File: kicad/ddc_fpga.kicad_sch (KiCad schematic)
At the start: 10 parts, among them U13 ICE40UP5K-SG48ITR

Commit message: updates
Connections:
- net CLK_DDC: now reaches U13.35 (IOT_46b_G0)
- net TOS_MARK_DDC: now reaches U13.37 (IOT_45a_G1)
- net DDC_I2S_WS: now reaches U13.10 (IOB_18a)
- net DDC_I2S_SD: now reaches U13.11 (IOB_20a)
- net DDC_RESET_L: now reaches U13.20 (IOB_25b_G3)
- net DDC_I2S_SCK: now reaches U13.9 (IOB_16a)
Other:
- moved on the sheet: C31, U13A
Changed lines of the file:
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@@
   (junction (at 147.32 147.32) (diameter 0) (color 0 0 0 0)
   )
-  (junction (at 44.45 115.57) (diameter 0) (color 0 0 0 0)
+  (junction (at 62.23 115.57) (diameter 0) (color 0 0 0 0)
   )
   (junction (at 101.6 151.13) (diameter 0) (color 0 0 0 0)
@@
   (junction (at 87.63 50.8) (diameter 0) (color 0 0 0 0)
   )
+  (wire (pts (xy 179.07 77.47) (xy 204.47 77.47))
+    (stroke (width 0) (type default))
+  )
   (wire (pts (xy 54.61 81.28) (xy 77.47 81.28))
     (stroke (width 0) (type default))
   )
+  (wire (pts (xy 179.07 80.01) (xy 204.47 80.01))
+    (stroke (width 0) (type default))
+  )
   (wire (pts (xy 118.11 132.08) (xy 118.11 153.67))
     (stroke (width 0) (type default))
@@
     (stroke (width 0) (type default))
   )
-  (wire (pts (xy 44.45 115.57) (xy 44.45 128.27))
+  (wire (pts (xy 62.23 115.57) (xy 62.23 128.27))
     (stroke (width 0) (type default))
   )
@@
     (stroke (width 0) (type default))
   )
-  (wire (pts (xy 50.8 115.57) (xy 44.45 115.57))
+  (wire (pts (xy 68.58 115.57) (xy 62.23 115.57))
     (stroke (width 0) (type default))
   )
@@
     (stroke (width 0) (type default))
   )
-  (wire (pts (xy 50.8 116.84) (xy 50.8 115.57))
+  (wire (pts (xy 68.58 116.84) (xy 68.58 115.57))
     (stroke (width 0) (type default))
   )
@@
     (stroke (width 0) (type default))
   )
+  (wire (pts (xy 36.83 161.29) (xy 52.07 161.29))
+    (stroke (width 0) (type default))
+  )
   (wire (pts (xy 123.19 132.08) (xy 118.11 132.08))
     (stroke (width 0) (type default))
@@
     (stroke (width 0) (type default))
   )
-  (wire (pts (xy 44.45 114.3) (xy 44.45 115.57))
+  (wire (pts (xy 179.07 90.17) (xy 204.47 90.17))
+    (stroke (width 0) (type default))
+  )
+  (wire (pts (xy 62.23 114.3) (xy 62.23 115.57))
     (stroke (width 0) (type default))
   )
@@
   )
   (wire (pts (xy 172.72 43.18) (xy 172.72 41.91))
+    (stroke (width 0) (type default))
+  )
+  (wire (pts (xy 36.83 163.83) (xy 52.07 163.83))
+    (stroke (width 0) (type default))
+  )
+  (wire (pts (xy 179.07 74.93) (xy 204.47 74.93))
     (stroke (width 0) (type default))
   )
@@
   (label "DDC_MISO_OUT" (at 181.61 97.79 0) (fields_autoplaced)
     (effects (font (size 1.27 1.27)) (justify left bottom))
+  )
+  (global_label "DDC_RESET_L" (shape input) (at 204.47 90.17 0) (fields_autoplaced)
+    (effects (font (size 1.27 1.27)) (justify left))
+    (property "Intersheetrefs" "${INTERSHEET_REFS}" (at 219.9736 90.17 0)
+      (effects (font (size 1.27 1.27)) (justify left) hide)
+    )
   )
   (global_label "DDC_SCK" (shape input) (at 208.28 102.87 0) (fields_autoplaced)
@@
     )
   )
+  (global_label "CLK_DDC" (shape input) (at 36.83 163.83 180) (fields_autoplaced)
+    (effects (font (size 1.27 1.27)) (justify right))
+    (property "Intersheetrefs" "${INTERSHEET_REFS}" (at 25.4991 163.83 0)
+      (effects (font (size 1.27 1.27)) (justify right) hide)
+    )
+  )
+  (global_label "DDC_I2S_WS" (shape output) (at 204.47 77.47 0) (fields_autoplaced)
+    (effects (font (size 1.27 1.27)) (justify left))
+    (property "Intersheetrefs" "${INTERSHEET_REFS}" (at 218.8851 77.47 0)
+      (effects (font (size 1.27 1.27)) (justify left) hide)
+    )
+  )
   (global_label "DDC_CRST" (shape input) (at 204.47 64.77 0) (fields_autoplaced)
     (effects (font (size 1.27 1.27)) (justify left))
@@
     )
   )
+  (global_label "DDC_I2S_SCK" (shape output) (at 204.47 74.93 0) (fields_autoplaced)
+    (effects (font (size 1.27 1.27)) (justify left))
+    (property "Intersheetrefs" "${INTERSHEET_REFS}" (at 219.9737 74.93 0)
+      (effects (font (size 1.27 1.27)) (justify left) hide)
+    )
+  )
   (global_label "ADC_SCK_P" (shape input) (at 54.61 78.74 180) (fields_autoplaced)
     (effects (font (size 1.27 1.27)) (justify right))
@@
     )
   )
+  (global_label "DDC_I2S_SD" (shape output) (at 204.47 80.01 0) (fields_autoplaced)
+    (effects (font (size 1.27 1.27)) (justify left))
+    (property "Intersheetrefs" "${INTERSHEET_REFS}" (at 218.7037 80.01 0)
+      (effects (font (size 1.27 1.27)) (justify left) hide)
+    )
+  )
   (global_label "ADC_SCK_N" (shape input) (at 54.61 81.28 180) (fields_autoplaced)
     (effects (font (size 1.27 1.27)) (justify right))
     (property "Intersheetrefs" "${INTERSHEET_REFS}" (at 40.981 81.28 0)
+      (effects (font (size 1.27 1.27)) (justify right) hide)
+    )
+  )
+  (global_label "TOS_MARK_DDC" (shape input) (at 36.83 161.29 180) (fields_autoplaced)
+    (effects (font (size 1.27 1.27)) (justify right))
+    (property "Intersheetrefs" "${INTERSHEET_REFS}" (at 19.512 161.29 0)
       (effects (font (size 1.27 1.27)) (justify right) hide)
     )
@@
   )
   (symbol (lib_id "Device:R_US") (at 199.39 97.79 90) (unit 1)
-    (in_bom yes) (on_board yes) (dnp no) (fields_autoplaced)
-    (property "Reference" "R23" (at 199.39 91.44 90)
-      (effects (font (size 1.27 1.27)))
-    )
-    (property "Value" "22" (at 199.39 93.98 90)
+    (in_bom yes) (on_board yes) (dnp no)
+    (property "Reference" "R23" (at 199.39 92.71 90)
+      (effects (font (size 1.27 1.27)))
+    )
+    (property "Value" "22" (at 199.39 95.25 90)
       (effects (font (size 1.27 1.27)))
     )
@@
     )
   )
-  (symbol (lib_id "power:+3.3V") (at 44.45 114.3 0) (unit 1)
-    (in_bom yes) (on_board yes) (dnp no) (fields_autoplaced)
-    (property "Reference" "#PWR068" (at 44.45 118.11 0)
-      (effects (font (size 1.27 1.27)) hide)
-    )
-    (property "Value" "+3.3V" (at 44.45 109.22 0)
-      (effects (font (size 1.27 1.27)))
-    )
-    (property "Footprint" "" (at 44.45 114.3 0)
-      (effects (font (size 1.27 1.27)) hide)
-    )
-    (property "Datasheet" "" (at 44.45 114.3 0)
+  (symbol (lib_id "power:+3.3V") (at 62.23 114.3 0) (unit 1)
+    (in_bom yes) (on_board yes) (dnp no) (fields_autoplaced)
+    (property "Reference" "#PWR068" (at 62.23 118.11 0)
+      (effects (font (size 1.27 1.27)) hide)
+    )
+    (property "Value" "+3.3V" (at 62.23 109.22 0)
+      (effects (font (size 1.27 1.27)))
+    )
+    (property "Footprint" "" (at 62.23 114.3 0)
+      (effects (font (size 1.27 1.27)) hide)
+    )
+    (property "Datasheet" "" (at 62.23 114.3 0)
       (effects (font (size 1.27 1.27)) hide)
     )
@@
     )
   )
-  (symbol (lib_id "FPGA_Lattice:ICE40UP5K-SG48ITR") (at 44.45 156.21 0) (unit 1)
-    (in_bom yes) (on_board yes) (dnp no) (fields_autoplaced)
-    (property "Reference" "U13" (at 53.34 156.21 0)
-      (effects (font (size 1.27 1.27)) (justify left))
-    )
-    (property "Value" "ICE40UP5K-SG48ITR" (at 53.34 158.75 0)
-      (effects (font (size 1.27 1.27)) (justify left))
-    )
-    (property "Footprint" "Package_DFN_QFN:QFN-48-1EP_7x7mm_P0.5mm_EP5.1x5.1mm" (at 44.45 190.5 0)
-      (effects (font (size 1.27 1.27)) hide)
-    )
-    (property "Datasheet" "http://www.latticesemi.com/Products/FPGAandCPLD/iCE40Ultra" (at 34.29 130.81 0)
+  (symbol (lib_id "FPGA_Lattice:ICE40UP5K-SG48ITR") (at 62.23 156.21 0) (unit 1)
+    (in_bom yes) (on_board yes) (dnp no) (fields_autoplaced)
+    (property "Reference" "U13" (at 71.12 156.21 0)
+      (effects (font (size 1.27 1.27)) (justify left))
+    )
+    (property "Value" "ICE40UP5K-SG48ITR" (at 71.12 158.75 0)
+      (effects (font (size 1.27 1.27)) (justify left))
+    )
+    (property "Footprint" "Package_DFN_QFN:QFN-48-1EP_7x7mm_P0.5mm_EP5.1x5.1mm" (at 62.23 190.5 0)
+      (effects (font (size 1.27 1.27)) hide)
+    )
+    (property "Datasheet" "http://www.latticesemi.com/Products/FPGAandCPLD/iCE40Ultra" (at 52.07 130.81 0)
       (effects (font (size 1.27 1.27)) hide)
     )
@@
     )
   )
-  (symbol (lib_id "power:GND") (at 50.8 124.46 0) (unit 1)
-    (in_bom yes) (on_board yes) (dnp no) (fields_autoplaced)
-    (property "Reference" "#PWR069" (at 50.8 130.81 0)
-      (effects (font (size 1.27 1.27)) hide)
-    )
-    (property "Value" "GND" (at 50.8 129.54 0)
-      (effects (font (size 1.27 1.27)) hide)
-    )
-    (property "Footprint" "" (at 50.8 124.46 0)
-      (effects (font (size 1.27 1.27)) hide)
-    )
-    (property "Datasheet" "" (at 50.8 124.46 0)
+  (symbol (lib_id "power:GND") (at 68.58 124.46 0) (unit 1)
+    (in_bom yes) (on_board yes) (dnp no) (fields_autoplaced)
+    (property "Reference" "#PWR069" (at 68.58 130.81 0)
+      (effects (font (size 1.27 1.27)) hide)
+    )
+    (property "Value" "GND" (at 68.58 129.54 0)
+      (effects (font (size 1.27 1.27)) hide)
+    )
+    (property "Footprint" "" (at 68.58 124.46 0)
+      (effects (font (size 1.27 1.27)) hide)
+    )
+    (property "Datasheet" "" (at 68.58 124.46 0)
       (effects (font (size 1.27 1.27)) hide)
     )
@@
     )
   )
-  (symbol (lib_id "Device:C") (at 50.8 120.65 0) (unit 1)
-    (in_bom yes) (on_board yes) (dnp no) (fields_autoplaced)
-    (property "Reference" "C31" (at 54.61 119.38 0)
-      (effects (font (size 1.27 1.27)) (justify left))
-    )
-    (property "Value" "4.7u" (at 54.61 121.92 0)
-      (effects (font (size 1.27 1.27)) (justify left))
-    )
-    (property "Footprint" "" (at 51.7652 124.46 0)
-      (effects (font (size 1.27 1.27)) hide)
-    )
-    (property "Datasheet" "~" (at 50.8 120.65 0)
-      (effects (font (size 1.27 1.27)) hide)
-    )
+  (symbol (lib_id "Device:C") (at 68.58 120.65 0) (unit 1)
+    (in_bom yes) (on_board yes) (dnp no) (fields_autoplaced)
+    (property "Reference" "C31" (at 72.39 119.38 0)
+      (effects (font (size 1.27 1.27)) (justify left))
+    )
+    (property "Value" "4.7u" (at 72.39 121.92 0)
+      (effects (font (size 1.27 1.27)) (justify left))
+    )
+    (property "Footprint" "" (at 69.5452 124.46 0)
+      (effects (font (size 1.27 1.27)) hide)
+    )
+    (property "Datasheet" "~" (at 68.58 120.65 0)
+      (effects (font (size 1.27 1.27)) hide)
+    )

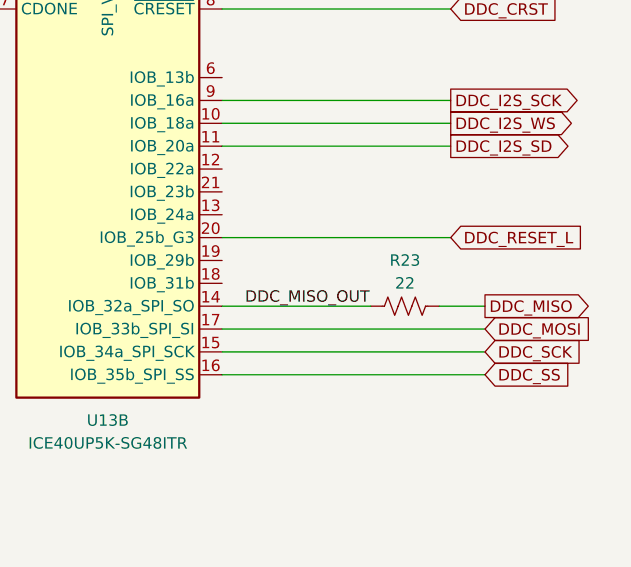
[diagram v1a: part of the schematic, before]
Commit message: wire up mcu
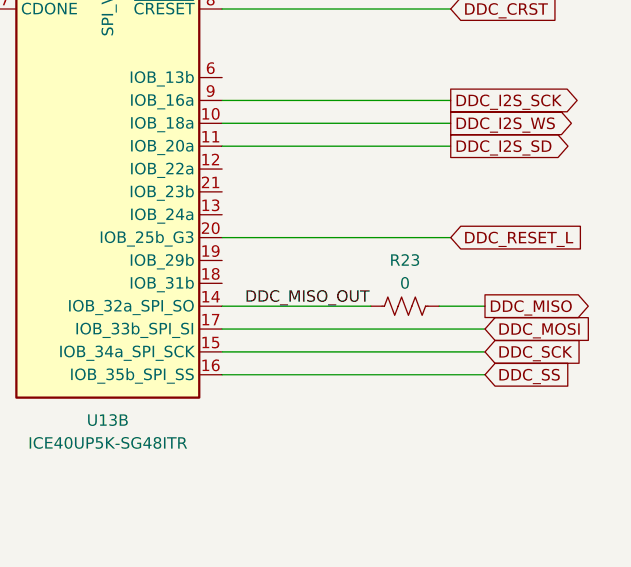
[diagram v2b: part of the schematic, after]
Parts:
- R23: value 22 -> 0
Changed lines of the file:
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@@
       (effects (font (size 1.27 1.27)))
     )
-    (property "Value" "22" (at 199.39 95.25 90)
+    (property "Value" "0" (at 199.39 95.25 90)
       (effects (font (size 1.27 1.27)))
     )

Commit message: fix ercs
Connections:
- net DDC_CRST renamed DDC_CRST_L
- no-connect marks 0 -> 24
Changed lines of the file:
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@@
   (junction (at 87.63 50.8) (diameter 0) (color 0 0 0 0)
   )
+  (no_connect (at 52.07 171.45))
+  (no_connect (at 52.07 148.59))
+  (no_connect (at 52.07 173.99))
+  (no_connect (at 52.07 156.21))
+  (no_connect (at 52.07 166.37))
+  (no_connect (at 77.47 91.44))
+  (no_connect (at 52.07 143.51))
+  (no_connect (at 77.47 93.98))
+  (no_connect (at 179.07 72.39))
+  (no_connect (at 52.07 140.97))
+  (no_connect (at 179.07 82.55))
+  (no_connect (at 179.07 87.63))
+  (no_connect (at 52.07 146.05))
+  (no_connect (at 179.07 85.09))
+  (no_connect (at 179.07 92.71))
+  (no_connect (at 52.07 158.75))
+  (no_connect (at 52.07 176.53))
+  (no_connect (at 52.07 181.61))
+  (no_connect (at 52.07 168.91))
+  (no_connect (at 52.07 153.67))
+  (no_connect (at 179.07 95.25))
+  (no_connect (at 52.07 179.07))
+  (no_connect (at 52.07 151.13))
+  (no_connect (at 77.47 88.9))
   (wire (pts (xy 179.07 77.47) (xy 204.47 77.47))
     (stroke (width 0) (type default))
@@
     )
   )
-  (global_label "DDC_CRST" (shape input) (at 204.47 64.77 0) (fields_autoplaced)
+  (global_label "DDC_CRST_L" (shape input) (at 204.47 64.77 0) (fields_autoplaced)
     (effects (font (size 1.27 1.27)) (justify left))
-    (property "Intersheetrefs" "${INTERSHEET_REFS}" (at 216.9499 64.77 0)
+    (property "Intersheetrefs" "${INTERSHEET_REFS}" (at 218.9456 64.77 0)
       (effects (font (size 1.27 1.27)) (justify left) hide)
     )

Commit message: power and frontend updates
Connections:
- net +3.3V renamed +3.3VP
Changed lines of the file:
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@@
     )
   )
-  (symbol (lib_id "power:+3.3V") (at 166.37 40.64 0) (unit 1)
+  (symbol (lib_id "power:+3.3VP") (at 62.23 114.3 0) (unit 1)
     (in_bom yes) (on_board yes) (dnp no) (fields_autoplaced)
-    (property "Reference" "#PWR066" (at 166.37 44.45 0)
+    (property "Reference" "#PWR068" (at 66.04 115.57 0)
       (effects (font (size 1.27 1.27)) hide)
     )
-    (property "Value" "+3.3V" (at 166.37 35.56 0)
+    (property "Value" "+3.3VP" (at 62.23 109.22 0)
+      (effects (font (size 1.27 1.27)))
+    )
+    (property "Footprint" "" (at 62.23 114.3 0)
+      (effects (font (size 1.27 1.27)) hide)
+    )
+    (property "Datasheet" "" (at 62.23 114.3 0)
+      (effects (font (size 1.27 1.27)) hide)
+    )
+    (pin "1")
+    (instances
+      (project "gpsrx"
+        (path "/c3c549bc-9d82-4b6a-bdb9-a3870905229d/c7ab4c42-2f90-4fd3-a6d5-50b84165476b"
+          (reference "#PWR068") (unit 1)
+        )
+      )
+    )
+  )
+  (symbol (lib_id "power:+3.3VP") (at 166.37 40.64 0) (unit 1)
+    (in_bom yes) (on_board yes) (dnp no) (fields_autoplaced)
+    (property "Reference" "#PWR066" (at 170.18 41.91 0)
+      (effects (font (size 1.27 1.27)) hide)
+    )
+    (property "Value" "+3.3VP" (at 166.37 35.56 0)
       (effects (font (size 1.27 1.27)))
     )
@@
         )
       )
-    )
-  )
-  (symbol (lib_id "power:+3.3V") (at 62.23 114.3 0) (unit 1)
-    (in_bom yes) (on_board yes) (dnp no) (fields_autoplaced)
-    (property "Reference" "#PWR068" (at 62.23 118.11 0)
-      (effects (font (size 1.27 1.27)) hide)
-    )
-    (property "Value" "+3.3V" (at 62.23 109.22 0)
-      (effects (font (size 1.27 1.27)))
-    )
-    (property "Footprint" "" (at 62.23 114.3 0)
-      (effects (font (size 1.27 1.27)) hide)
-    )
-    (property "Datasheet" "" (at 62.23 114.3 0)
-      (effects (font (size 1.27 1.27)) hide)
-    )
-    (pin "1")
-    (instances
-      (project "gpsrx"
-        (path "/c3c549bc-9d82-4b6a-bdb9-a3870905229d/c7ab4c42-2f90-4fd3-a6d5-50b84165476b"
-          (reference "#PWR068") (unit 1)
-        )
-      )

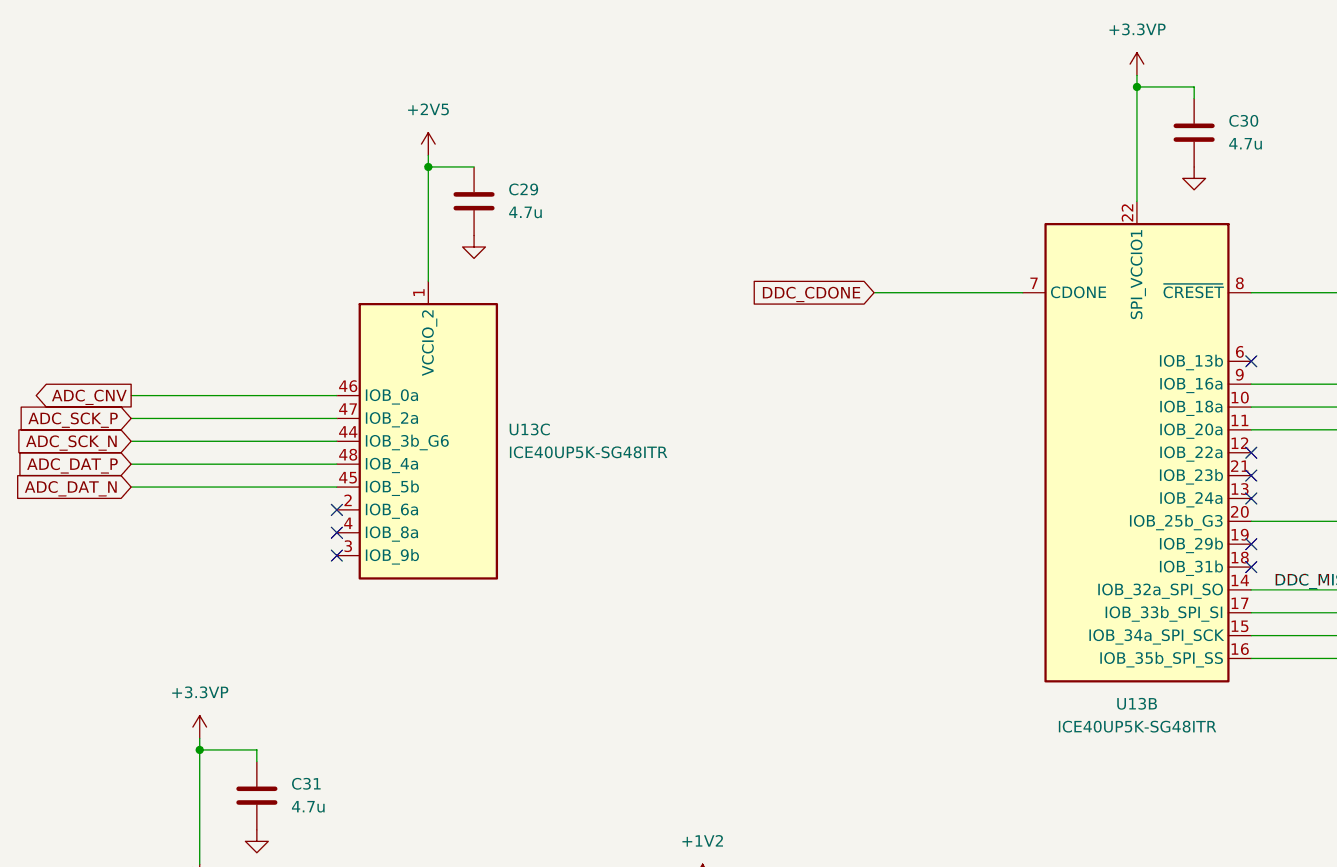
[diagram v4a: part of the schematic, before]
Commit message: swap ice40 for max v, add 1.2v switcher
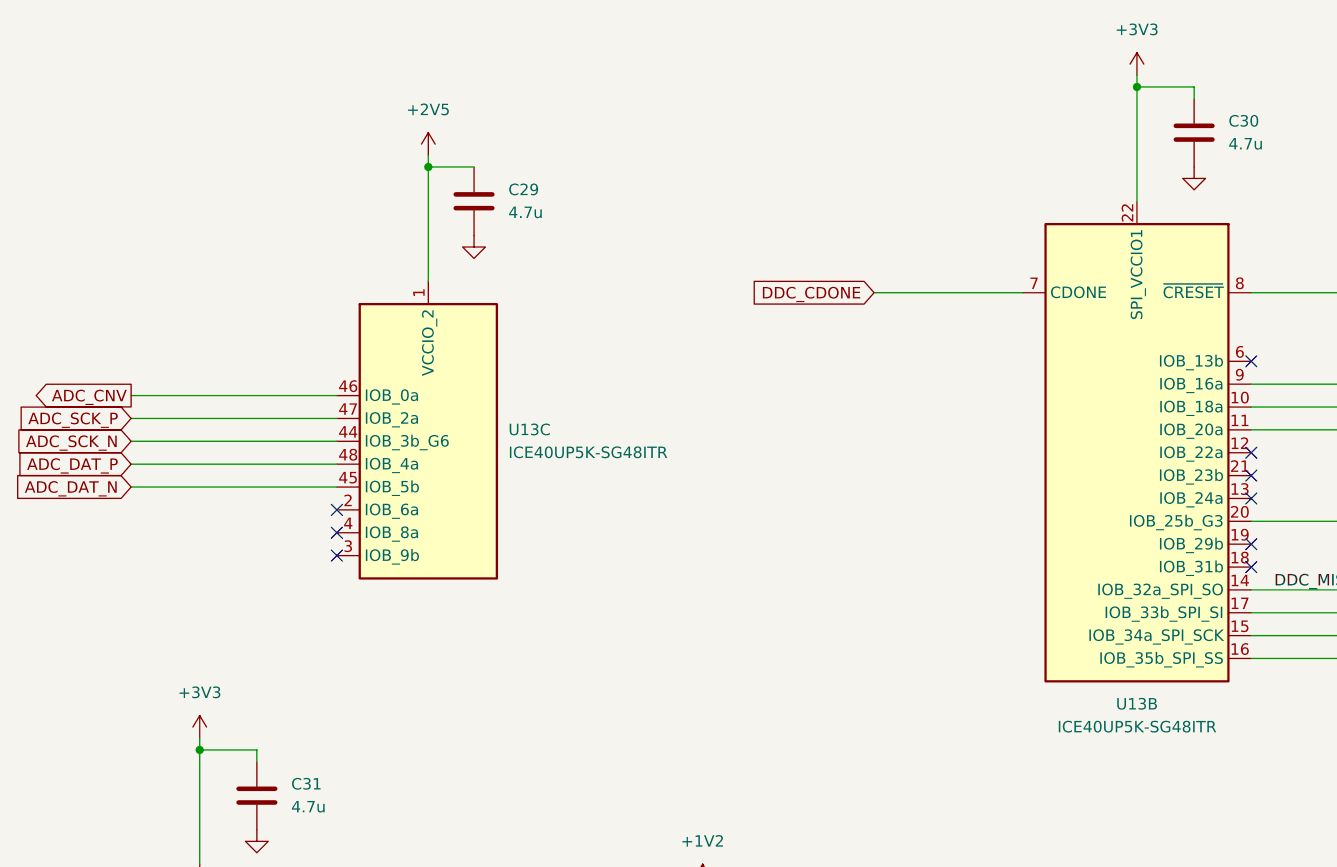
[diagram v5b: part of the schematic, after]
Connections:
- net +3.3VP renamed +3V3
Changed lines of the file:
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@@
     )
   )
-  (symbol (lib_id "power:+3.3VP") (at 62.23 114.3 0) (unit 1)
-    (in_bom yes) (on_board yes) (dnp no) (fields_autoplaced)
-    (property "Reference" "#PWR068" (at 66.04 115.57 0)
-      (effects (font (size 1.27 1.27)) hide)
-    )
-    (property "Value" "+3.3VP" (at 62.23 109.22 0)
+  (symbol (lib_id "power:+3V3") (at 62.23 114.3 0) (unit 1)
+    (in_bom yes) (on_board yes) (dnp no) (fields_autoplaced)
+    (property "Reference" "#PWR068" (at 62.23 118.11 0)
+      (effects (font (size 1.27 1.27)) hide)
+    )
+    (property "Value" "+3V3" (at 62.23 109.22 0)
       (effects (font (size 1.27 1.27)))
     )
@@
         (path "/c3c549bc-9d82-4b6a-bdb9-a3870905229d/c7ab4c42-2f90-4fd3-a6d5-50b84165476b"
           (reference "#PWR068") (unit 1)
-        )
-      )
-    )
-  )
-  (symbol (lib_id "power:+3.3VP") (at 166.37 40.64 0) (unit 1)
-    (in_bom yes) (on_board yes) (dnp no) (fields_autoplaced)
-    (property "Reference" "#PWR066" (at 170.18 41.91 0)
-      (effects (font (size 1.27 1.27)) hide)
-    )
-    (property "Value" "+3.3VP" (at 166.37 35.56 0)
-      (effects (font (size 1.27 1.27)))
-    )
-    (property "Footprint" "" (at 166.37 40.64 0)
-      (effects (font (size 1.27 1.27)) hide)
-    )
-    (property "Datasheet" "" (at 166.37 40.64 0)
-      (effects (font (size 1.27 1.27)) hide)
-    )
-    (pin "1")
-    (instances
-      (project "gpsrx"
-        (path "/c3c549bc-9d82-4b6a-bdb9-a3870905229d/c7ab4c42-2f90-4fd3-a6d5-50b84165476b"
-          (reference "#PWR066") (unit 1)
         )
       )
@@
         )
       )
+    )
+  )
+  (symbol (lib_id "power:+3V3") (at 166.37 40.64 0) (unit 1)
+    (in_bom yes) (on_board yes) (dnp no) (fields_autoplaced)
+    (property "Reference" "#PWR066" (at 166.37 44.45 0)
+      (effects (font (size 1.27 1.27)) hide)
+    )
+    (property "Value" "+3V3" (at 166.37 35.56 0)
+      (effects (font (size 1.27 1.27)))
+    )
+    (property "Footprint" "" (at 166.37 40.64 0)
+      (effects (font (size 1.27 1.27)) hide)
+    )
+    (property "Datasheet" "" (at 166.37 40.64 0)
+      (effects (font (size 1.27 1.27)) hide)
+    )
+    (pin "1")
+    (instances
+      (project "gpsrx"
+        (path "/c3c549bc-9d82-4b6a-bdb9-a3870905229d/c7ab4c42-2f90-4fd3-a6d5-50b84165476b"
+          (reference "#PWR066") (unit 1)
+        )
+      )
